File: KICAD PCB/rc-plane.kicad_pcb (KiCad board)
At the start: 4 copper layers, 65 x 56 mm, 138 parts, among them J1 POWER, J2 ARMING_PLUG, J3 SMA, J4 E-MATCH_DROGUE, J5 SWD, J6 E-MATCH_RECOVERY, J7 USB4105-GF-A, J8 E-MATCH_BACKUP, J9 HTSW-109-08-T-T-RA, Q1 Q_NMOS_GSD, Q2 Q_NMOS_GSD, Q4 Q_NMOS_GSD, Q5 Q_NMOS_GSD, Q6 Q_NMOS_GSD, Q7 Q_NMOS_GSD, U10 RASPBERRY_PI_4B_4GB, U11 STM32F105RCT6, U12 MP2338GTL-Z, U13 MP2338GTL-Z, U2 RFM95W, U3 SAM-M8Q-0, U46 W25N01GVZEIG TR, U5 MP2338GTL-Z, U6 BMI088, U7 MS5607-02BA03, U8 BMM350, U9 USBLC6-2SC6, Y1 16MHz

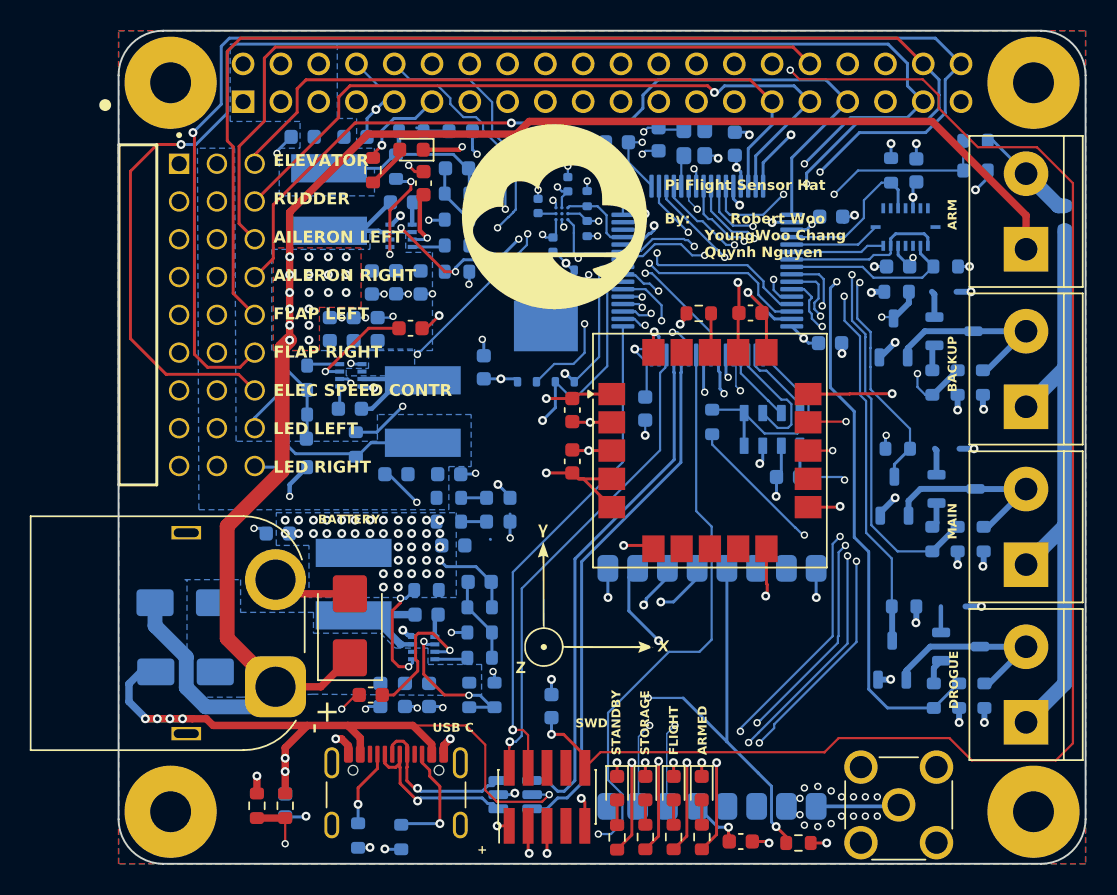
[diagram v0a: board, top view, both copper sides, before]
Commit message: working on rev2 on the board, deving out code for flight for stm32 software
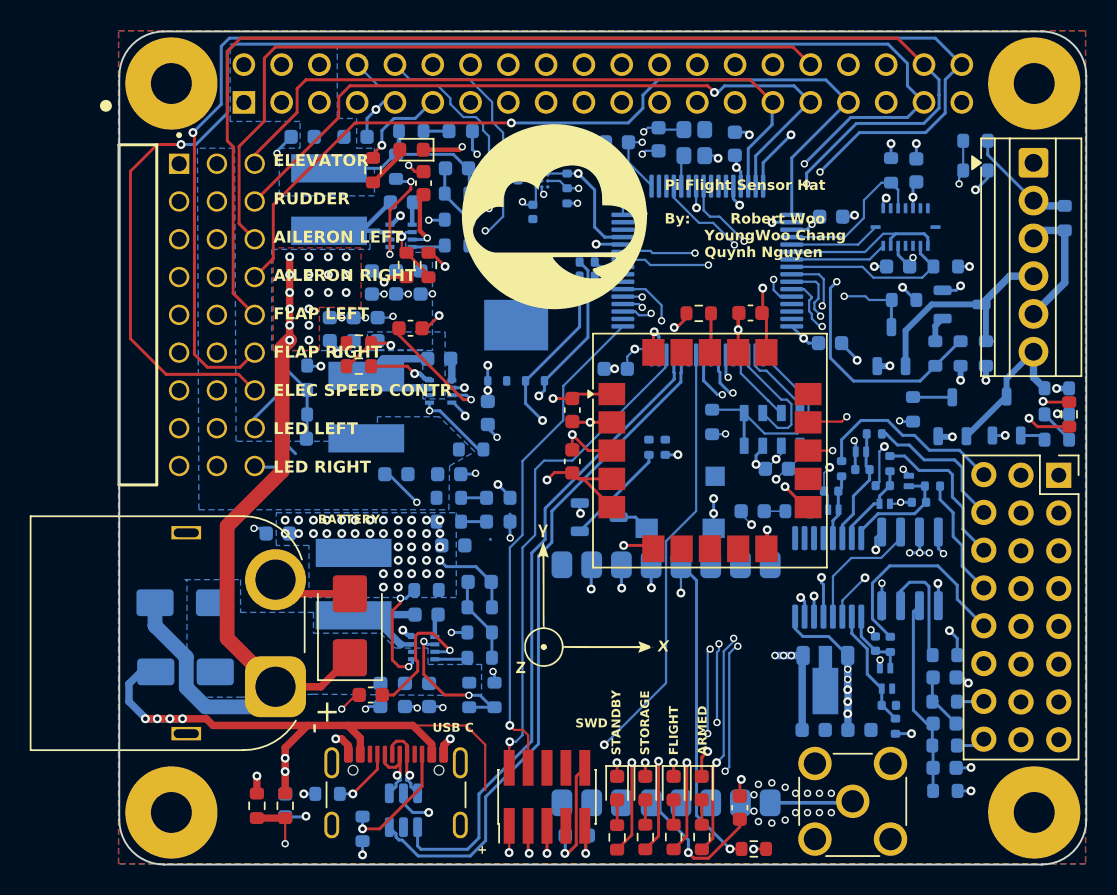
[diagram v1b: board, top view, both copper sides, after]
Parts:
- removed J6: E-MATCH_RECOVERY, TerminalBlock:TerminalBlock_bornier-2_P5.08mm
- removed J8: E-MATCH_BACKUP, TerminalBlock:TerminalBlock_bornier-2_P5.08mm
- removed Q7: Q_NMOS_GSD, Package_TO_SOT_SMD:TSOT-23
- added C10: 100nF, Capacitor_SMD:C_0402_1005Metric, B.Cu at (128.9, 90.2)
- added C11: 100nF, Capacitor_SMD:C_0402_1005Metric, B.Cu at (125.9, 80.0)
- added C12: 100nF, Capacitor_SMD:C_0402_1005Metric, B.Cu at (129.8, 94.3)
- added C13: 0.33uF, Capacitor_SMD:C_0603_1608Metric, B.Cu at (124.7, 96.0)
- added C16: 0.1uF, Capacitor_SMD:C_0603_1608Metric, B.Cu at (127.8, 96.0)
- added C17: 10nF, Capacitor_SMD:C_0603_1608Metric, B.Cu at (133.5, 98.5)
- added C18: 0.1uF, Capacitor_SMD:C_0603_1608Metric, B.Cu at (120.6, 81.3)
- added C19: 10nF, Capacitor_SMD:C_0603_1608Metric, B.Cu at (133.5, 92.5)
- added C2: 100nF, Capacitor_SMD:C_0402_1005Metric, B.Cu at (128.0, 78.5)
- added C20: 33nF, Capacitor_SMD:C_0603_1608Metric, B.Cu at (133.5, 95.6)
- added C3: 100nF, Capacitor_SMD:C_0402_1005Metric, B.Cu at (129.4, 79.6)
- added C8: 100nF, Capacitor_SMD:C_0402_1005Metric, B.Cu at (131.8, 80.7)
- added D14: 3.9V, Diode_SMD:D_SOD-882, B.Cu at (131.1, 79.3)
- added D15: 3.9V, Diode_SMD:D_SOD-882, B.Cu at (129.5, 91.8)
- added D16: 3.9V, Diode_SMD:D_SOD-882, B.Cu at (126.0, 81.2)
- added D17: 3.9V, Diode_SMD:D_SOD-882, B.Cu at (129.7, 93.2)
- added D6: 3.9V, Diode_SMD:D_SOD-882, B.Cu at (127.9, 77.3)
- added D9: 3.9V, Diode_SMD:D_SOD-882, B.Cu at (129.5, 80.8)
- added J10: Conn_01x06_Socket, TerminalBlock:TerminalBlock_Xinya_XY308-2.54-6P_1x06_P2.54mm_Horizontal, F.Cu at (139.5, 57.9)
- added R12: 80k, Resistor_SMD:R_0603_1608Metric, F.Cu at (98.8, 64.8)
- added R13: 200k, Resistor_SMD:R_0603_1608Metric, F.Cu at (94.2, 70.0)
- added R22: 80k, Resistor_SMD:R_0603_1608Metric, F.Cu at (94.2, 71.5)
- added R23: 1K, Resistor_SMD:R_0402_1005Metric, B.Cu at (128.8, 76.1)
- added R26: 1K, Resistor_SMD:R_0402_1005Metric, B.Cu at (129.8, 78.1)
- added R28: 1K, Resistor_SMD:R_0402_1005Metric, B.Cu at (132.7, 79.6)
- added R29: 1K, Resistor_SMD:R_0402_1005Metric, B.Cu at (129.9, 90.2)
- added R33: 1K, Resistor_SMD:R_0402_1005Metric, B.Cu at (130.2, 95.8)
- added R34: 165R, Resistor_SMD:R_0603_1608Metric, F.Cu at (141.9, 74.8)
- added R37: 100, Resistor_SMD:R_0402_1005Metric, B.Cu at (113.7, 77.0)
- added R8: 200k, Resistor_SMD:R_0603_1608Metric, F.Cu at (97.3, 64.8)
- added R94: 33K, Resistor_SMD:R_0603_1608Metric, B.Cu at (133.6, 100.1)
- added R96: 1k, Resistor_SMD:R_0603_1608Metric, B.Cu at (133.5, 94.1)
- added R97: 1k, Resistor_SMD:R_0603_1608Metric, B.Cu at (133.5, 97.0)
- added R98: 33K, Resistor_SMD:R_0603_1608Metric, B.Cu at (133.6, 91.0)
- added U1: MAX11614, Package_SO:QSOP-16_3.9x4.9mm_P0.635mm, B.Cu at (125.7, 85.7)
- added U33: AS78L05RTR, Package_TO_SOT_SMD:SOT-89-3, B.Cu at (125.5, 93.0)
- added U4: INA126, Package_SO:SOIC-8_3.9x4.9mm_P1.27mm, B.Cu at (131.2, 85.2)
- J2: value ARMING_PLUG -> 2.54mm 3x08 header; footprint TerminalBlock:TerminalBlock_bornier-2_P5.08mm -> UCIRP-KiCAD-Lib:HX PZ2.54-3x8P ZZ 3x08 2.54mm THT header
- J4: value E-MATCH_DROGUE -> ALARM; footprint TerminalBlock:TerminalBlock_bornier-2_P5.08mm -> UCIRP-KiCAD-Lib:XDCR_SMT-0540-S-R; moved to B.Cu
- R31: value 100k -> 1K; footprint Resistor_SMD:R_0603_1608Metric -> Resistor_SMD:R_0402_1005Metric
- R35: value 1k -> 2k
- R36: value 10k -> 10K; footprint Resistor_SMD:R_0603_1608Metric -> Resistor_SMD:R_0402_1005Metric
- R38: value 100 -> 22R; footprint Resistor_SMD:R_0603_1608Metric -> Resistor_SMD:R_0402_1005Metric
- R39: value 10k -> 22R; footprint Resistor_SMD:R_0603_1608Metric -> Resistor_SMD:R_0402_1005Metric
- R54: value 100k -> 22R; footprint Resistor_SMD:R_0603_1608Metric -> Resistor_SMD:R_0402_1005Metric
- moved R31 29.0 mm to (126.6, 78.4), turned to -90 degrees
- moved J4 27.5 mm to (115.8, 80.8), turned to 180 degrees
- moved R39 25.9 mm to (109.5, 65.5), turned to 180 degrees
- moved R38 24.0 mm to (109.5, 66.5), turned to 180 degrees
- moved R54 24.0 mm to (109.5, 64.5)
- moved Q6 23.2 mm to (110.3, 81.7), turned to 0 degrees
- moved Q2 23.0 mm to (134.7, 67.4)
- moved R5 23.0 mm to (136.3, 70.7)
- moved R6 23.0 mm to (132.9, 70.7)
- moved R7 23.0 mm to (134.6, 70.7)
- moved R36 21.8 mm to (114.8, 77.0), turned to 90 degrees
- moved Q1 21.1 mm to (129.9, 70.2)
- moved R4 20.6 mm to (130.8, 67.1)
- moved R35 16.2 mm to (123.7, 81.3)
- moved J2 15.2 mm to (138.7, 78.9), turned to 0 degrees
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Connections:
- net Net-(J6-Pin_2) renamed MAIN-
- C21 pad 2: /Buck1/FB -> +5V
- C26 pad 2: BATTERY -> ARM+
- C28 pad 2: BATTERY -> ARM+
- C31 pad 2: BATTERY -> ARM+
- C39 pad 2: BATTERY -> ARM+
- C40 pad 2: BATTERY -> ARM+
- C41 pad 2: BATTERY -> ARM+
- D1 pad 1: BATTERY -> ARM+
- D5 pad 2: BATTERY -> ARM+
- J1 pad 1: BATTERY -> GND
- J1 pad 2: GND -> ARM+
- J2 pad 1: BATTERY -> GND
- J2 pad 2: Net-(J2-Pin_2) -> GND
- J4 pad 1: ARM_POWER -> +3.3V
- Q1 pad 1: Net-(J4-Pin_2) -> DROGUE-
- Q2 pad 3: Net-(J4-Pin_2) -> DROGUE-
- Q5 pad 3: RECOVERY_CONT -> MAIN_CONT
- Q6 pad 1: Net-(J8-Pin_2) -> Net-(Q6-G)
- Q6 pad 3: BACKUP_CONT -> Net-(J4-Pin_2)
- R1 pad 1: Net-(J2-Pin_2) -> ARM-
- R11 pad 2: Net-(J2-Pin_2) -> ARM-
- R14 pad 1: RECOVERY -> MAIN
- R15 pad 1: RECOVERY -> MAIN
- R19 pad 2: RECOVERY_CONT -> MAIN_CONT
- R31 pad 1: EN_PI -> ADC_AIN1
- R31 pad 2: GND -> /Single_Ended_ADC/OUT
- R32 pad 1: /Buck1/FB -> +5V
- R35 pad 1: +3.3V -> Net-(C18-Pad2)
- R35 pad 2: BACKUP_CONT -> Net-(U1-REF)
- R36 pad 1: Net-(J8-Pin_2) -> GND
- R36 pad 2: GND -> ALARM
- R38 pad 1: Net-(Q7-G) -> Net-(U11-PB3)
- R38 pad 2: BACKUP -> MEM_SCK
- R39 pad 1: BACKUP -> Net-(U11-PB4)
- R39 pad 2: GND -> MEM_MISO
- R43 pad 1: /Buck1/FB -> +5V
- R46 pad 2: /Buck1/FB -> +5V
- R5 pad 1: Net-(J4-Pin_2) -> DROGUE-
- R54 pad 1: EN_SERVO -> Net-(U11-PB5)
- R54 pad 2: GND -> MEM_MOSI
- U10 pad 1: 3V3_1 -> 3V3
- U10 pad 17: 3V3 -> 3V3_1
- U10 pad S2: SHIELD_3 -> SHIELD_2
- U10 pad S4: SHIELD_2 -> SHIELD_3
- U11 pad 10: RECOVERY -> unconnected-(U11-PC2-Pad10)
- U11 pad 11: ARM_CONT -> unconnected-(U11-PC3-Pad11)
- U11 pad 2: BACKUP_CONT -> unconnected-(U11-PC13-Pad2)
- U11 pad 22: IMU_MOSI -> IMU_MISO
- U11 pad 23: IMU_MISO -> IMU_MOSI
- U11 pad 29: EN_SERVO -> unconnected-(U11-PB10-Pad29)
- U11 pad 3: BACKUP -> unconnected-(U11-PC14-Pad3)
- U11 pad 30: EN_PI -> unconnected-(U11-PB11-Pad30)
- U11 pad 37: RADIO_DIO1 -> unconnected-(U11-PC6-Pad37)
- U11 pad 40: MAG_INT -> unconnected-(U11-PC9-Pad40)
- U11 pad 43: MEM_WP -> unconnected-(U11-PA10-Pad43)
- U11 pad 50: MEM_HOLD -> unconnected-(U11-PA15-Pad50)
- U11 pad 55: MEM_SCK -> Net-(U11-PB3)
- U11 pad 56: MEM_MISO -> Net-(U11-PB4)
- U11 pad 57: MEM_MOSI -> Net-(U11-PB5)
- U11 pad 6: RADIO_DIO0 -> unconnected-(U11-PD1-Pad6)
- U11 pad 9: RECOVERY_CONT -> unconnected-(U11-PC1-Pad9)
- U12 pad 2: BATTERY -> ARM+
- U12 pad 6: EN_SERVO -> /Buck/EN
- U5 pad 2: BATTERY -> ARM+
- U5 pad 6: EN_PI -> /Buck1/EN
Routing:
- net ARM+: track 0.00 -> 190.8 mm, vias 0 -> 23
- net BATTERY: track 111.4 -> 0.00 mm, vias 18 -> 0
- net +5V_ADC: track 0.00 -> 50.9 mm, vias 0 -> 8
- net EN_SERVO: track 49.9 -> 0.00 mm, vias 5 -> 0
- net RADIO_DIO0: track 43.7 -> 0.00 mm, vias 2 -> 0
- net MAG_SCL: track 5.30 -> 46.8 mm, vias 0 -> 2
- net RECOVERY: track 37.3 -> 0.00 mm, vias 2 -> 0
- net RADIO_DIO1: track 35.1 -> 0.00 mm, vias 2 -> 0
- net MAG_SDA: track 6.59 -> 39.7 mm, vias 2 -> 3
- net ARM_POWER: track 41.7 -> 8.81 mm
- net EN_PI: track 32.7 -> 0.00 mm, vias 4 -> 0
- net RECOVERY_CONT: track 29.2 -> 0.00 mm, vias 2 -> 0
- net BACKUP: track 27.8 -> 0.00 mm, vias 2 -> 0
- net BACKUP_CONT: track 23.3 -> 0.00 mm, vias 2 -> 0
- net DROGUE: track 49.2 -> 29.0 mm
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- added copper zone on B.Cu, net ARM+
- added copper zone on F.Cu, net ARM+
- added copper zone on In2.Cu, net GND
- removed copper zone on B.Cu, net BATTERY
- removed copper zone on F.Cu, net BATTERY
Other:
- board text removed: "ARM"
- board text removed: "BACKUP"
- board text removed: "DROGUE"
- board text removed: "MAIN"

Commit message: moved to stm32cube vscode extension, v2.0 purchased
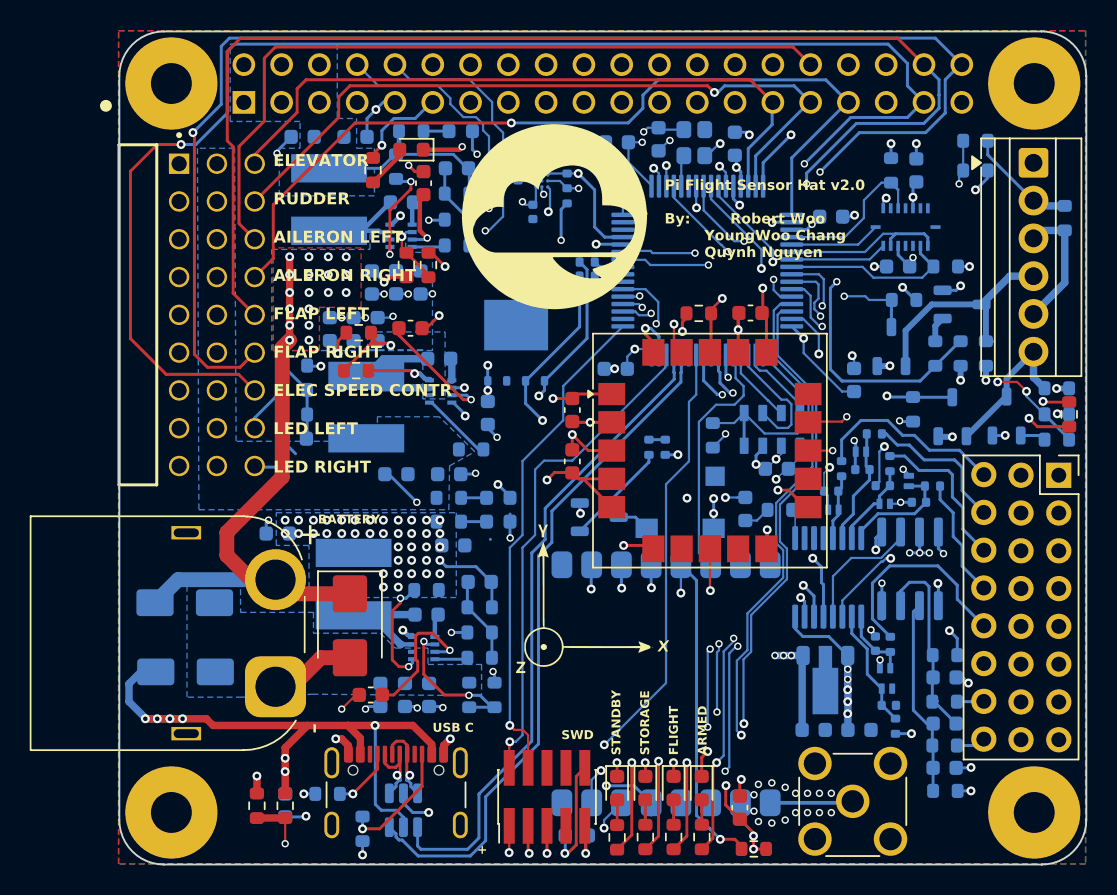
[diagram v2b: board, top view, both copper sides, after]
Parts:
- moved C34 2.96 mm to (127.4, 72.5), turned to 90 degrees
- moved R35 1.20 mm to (122.5, 81.2)
- moved R40 0.90 mm to (117.9, 76.2)
- moved R13 0.70 mm to (94.1, 69.3)
- moved C18 0.52 mm to (120.1, 81.2), turned to -90 degrees
- moved R22 0.35 mm to (94.0, 71.8)
- turned D1 to -90 degrees
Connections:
- net MAG_SCL renamed SCL
- net MAG_SDA renamed SDA
- C21 pad 2: +5V -> /Buck1/FB
- R32 pad 1: +5V -> /Buck1/FB
- R43 pad 1: +5V -> /Buck1/FB
- R46 pad 2: +5V -> /Buck1/FB
- U11 pad 10: unconnected-(U11-PC2-Pad10) -> MAIN
- U11 pad 11: unconnected-(U11-PC3-Pad11) -> MAG_INT
- U11 pad 2: unconnected-(U11-PC13-Pad2) -> GPS_INT
- U11 pad 29: unconnected-(U11-PB10-Pad29) -> RADIO_DIO0
- U11 pad 3: unconnected-(U11-PC14-Pad3) -> GPS_SAFEBOOT
- U11 pad 30: unconnected-(U11-PB11-Pad30) -> RADIO_DIO1
- U11 pad 37: unconnected-(U11-PC6-Pad37) -> RADIO_nRST
- U11 pad 40: unconnected-(U11-PC9-Pad40) -> GPS_RESET
- U11 pad 9: unconnected-(U11-PC1-Pad9) -> MAIN_CONT
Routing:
- net RADIO_DIO0: track 0.00 -> 48.0 mm, vias 0 -> 2
- net RADIO_DIO1: track 0.00 -> 45.6 mm, vias 0 -> 2
- net GPS_SAFEBOOT: track 0.00 -> 45.0 mm, vias 0 -> 2
- net MAIN: track 2.38 -> 31.7 mm, vias 0 -> 3
- net MAIN_CONT: track 2.65 -> 25.0 mm, vias 0 -> 2
- net GPS_INT: track 0.00 -> 22.4 mm, vias 0 -> 2
- net MAG_INT: track 0.00 -> 18.8 mm, vias 0 -> 2
- net RADIO_nRST: track 0.00 -> 16.7 mm
- net +3.3V: track 70.5 -> 85.2 mm, vias 69 -> 71
- net ARM+: track 190.8 -> 178.5 mm
- net GND: track 159.0 -> 166.3 mm, vias 115 -> 117
- net +5V: track 19.4 -> 13.6 mm
- net /Buck1/FB: track 0.00 -> 5.80 mm
- net GPS_RESET: track 2.68 -> 8.11 mm, vias 0 -> 1
- net Net-(U1-REF): track 0.00 -> 1.98 mm
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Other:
- board text added: "->"
- board text added: "Pi Flight Sensor Hat v2.0 By: Robert Woo YoungWoo Chang Quynh Nguyen"
- board text removed: "Pi Flight Sensor Hat By: Robert Woo YoungWoo Chang Quynh Nguyen"
